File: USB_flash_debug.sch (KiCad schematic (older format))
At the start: 31 parts, among them IC2 TPS7A0518PDBVT, J6 E8124-015-01, J9 E8124-015-01, Q7 BSS138-7-F, Q8 BSS138-7-F, SW1 1X03, U13 FT232RQ-REEL, U9 FSUSB30MUX

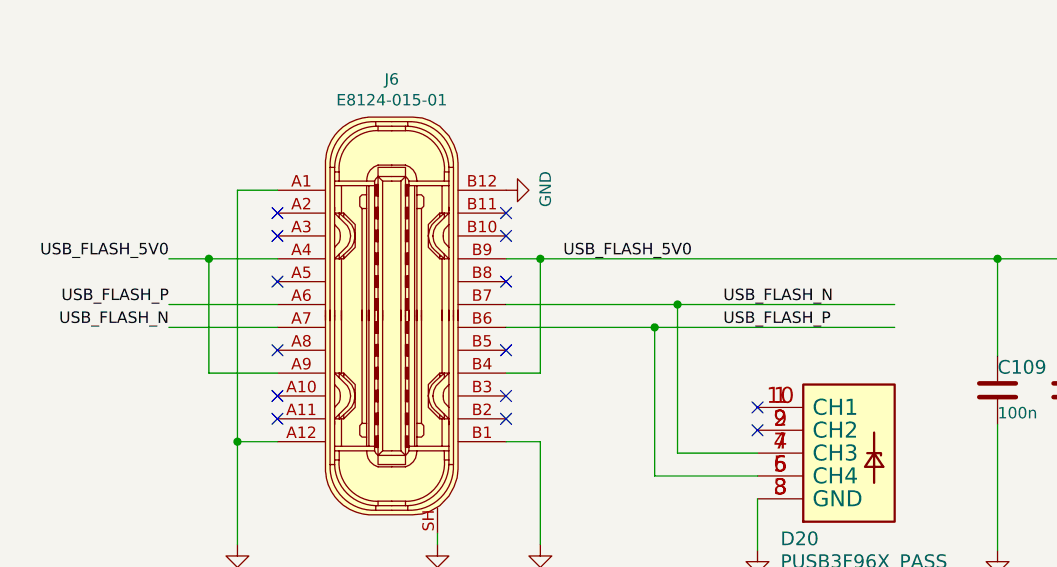
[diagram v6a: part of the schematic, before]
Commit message: Schematic cleanup-USB HUB
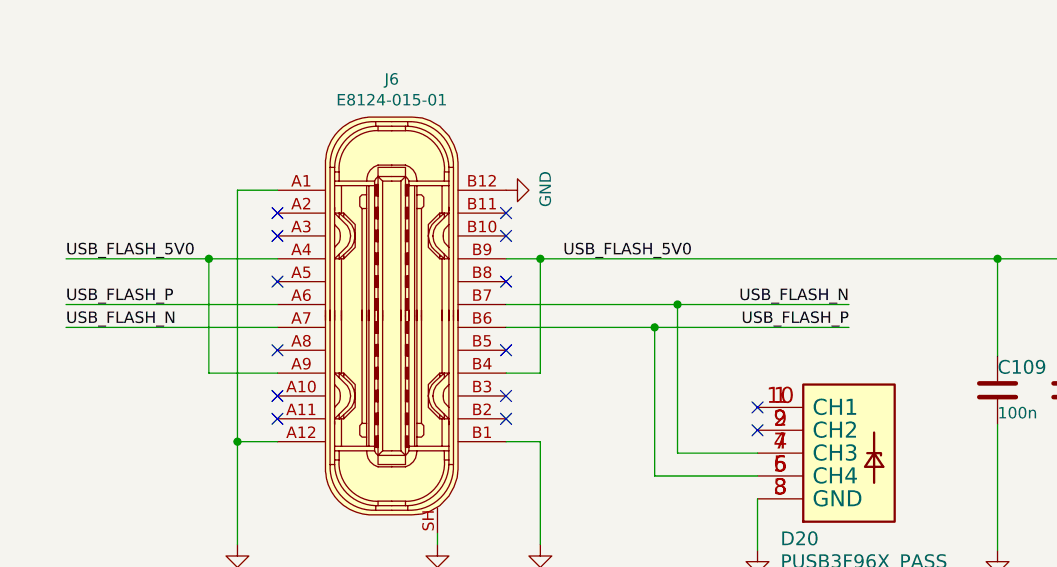
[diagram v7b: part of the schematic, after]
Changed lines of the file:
@@
 	3575 4525 3575 3875
 Wire Wire Line
-	3575 3875 4625 3875
-Wire Wire Line
-	4625 3775 3675 3775
+	3575 3875 4425 3875
+Wire Wire Line
+	4425 3775 3675 3775
 Text Notes 3525 1050 0    100  ~ 20
 USB SoM flashing IF
@@
 Text Label 10350 3575 0    50   ~ 0
 DBG_VBUS
-Text Label 3875 3875 0    50   ~ 0
+Text Label 4425 3875 2    50   ~ 0
 USB_FLASH_P
-Text Label 3875 3775 0    50   ~ 0
+Text Label 4425 3775 2    50   ~ 0
 USB_FLASH_N
 Text Label 3175 3575 0    50   ~ 0
@@
 	0    -1   -1   0
 $EndComp
-Text Label 1450 3575 2    50   ~ 0
+Text Label 1000 3575 0    50   ~ 0
 USB_FLASH_5V0
 Wire Wire Line
-	1450 3575 1625 3575
+	1000 3575 1625 3575
 NoConn ~ 4025 4225
 NoConn ~ 4025 4325
@@
 NoConn ~ 1925 3375
 Wire Wire Line
-	1925 3775 1450 3775
-Wire Wire Line
-	1450 3875 1925 3875
-Text Label 1450 3775 2    50   ~ 0
+	1925 3775 1000 3775
+Wire Wire Line
+	1000 3875 1925 3875
+Text Label 1000 3775 0    50   ~ 0
 USB_FLASH_P
-Text Label 1450 3875 2    50   ~ 0
+Text Label 1000 3875 0    50   ~ 0
 USB_FLASH_N
 $Comp
